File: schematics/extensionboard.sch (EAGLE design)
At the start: 25 parts, among them IC1 TXS0104E, IC2 TXS0104E, IC3 TXS0104E, IC4 TXS0104E, IC5 TXS0104E_ENA, J1 Raspberry Pi 3, J10 RPi_GPIO_2, J11 I2C_0, J12 SPI1_5V, J13 SDA1_5V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

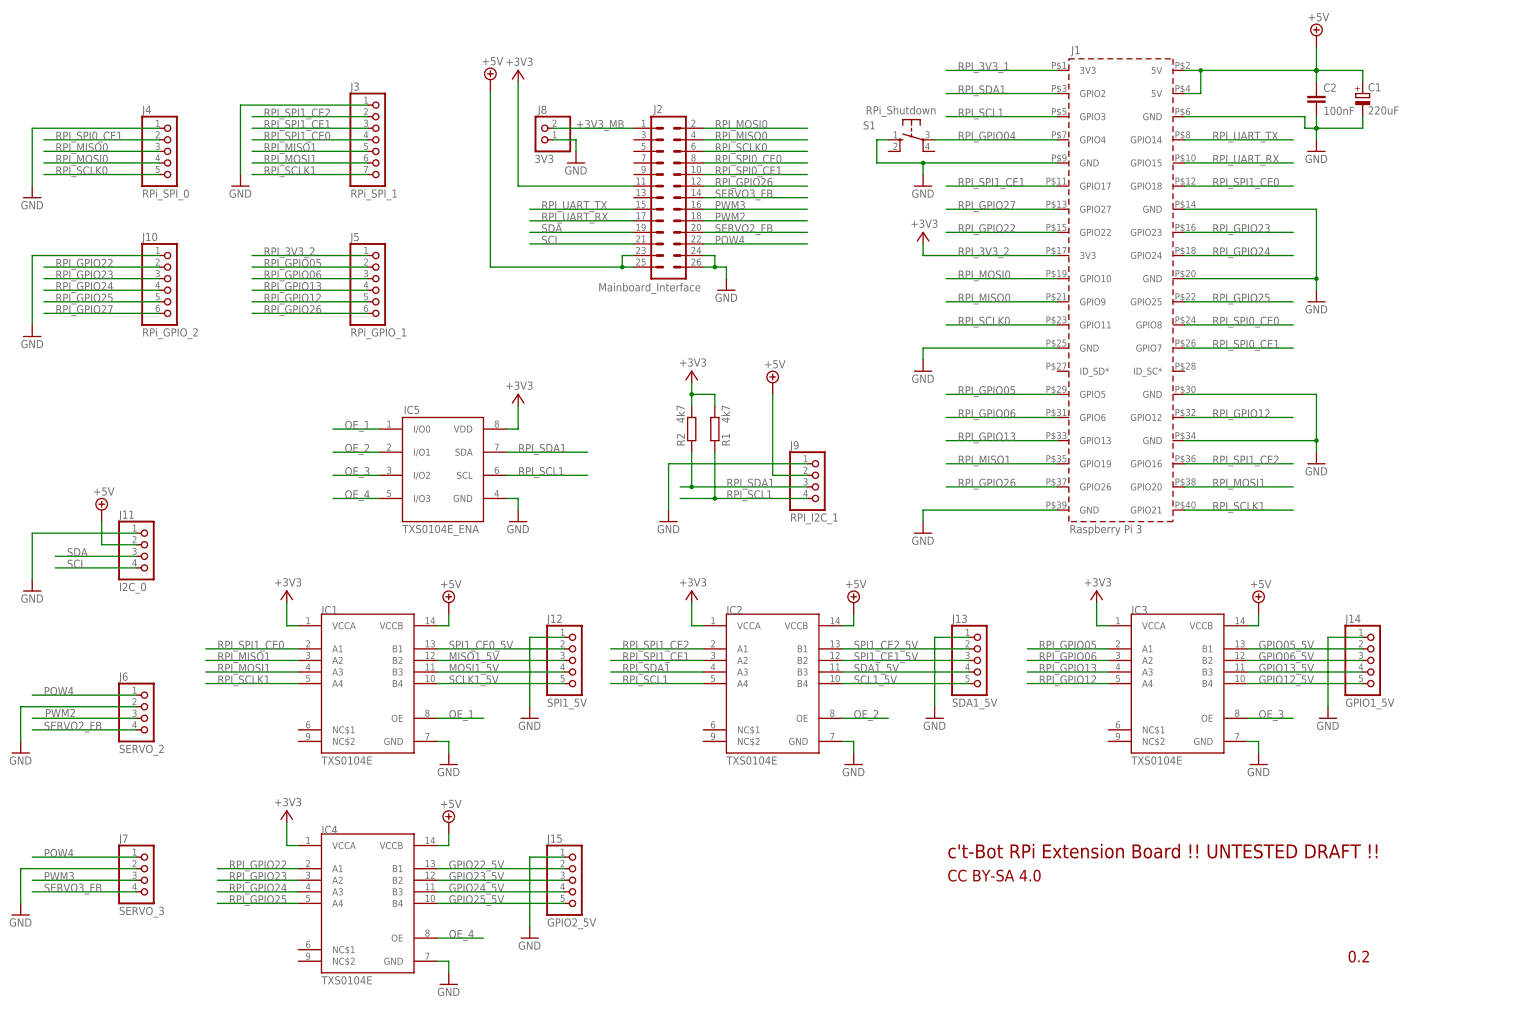
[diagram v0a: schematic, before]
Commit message: Servo PWM pullups corrected, battery voltage divider adjusted
schematic layout improved, signal names unified
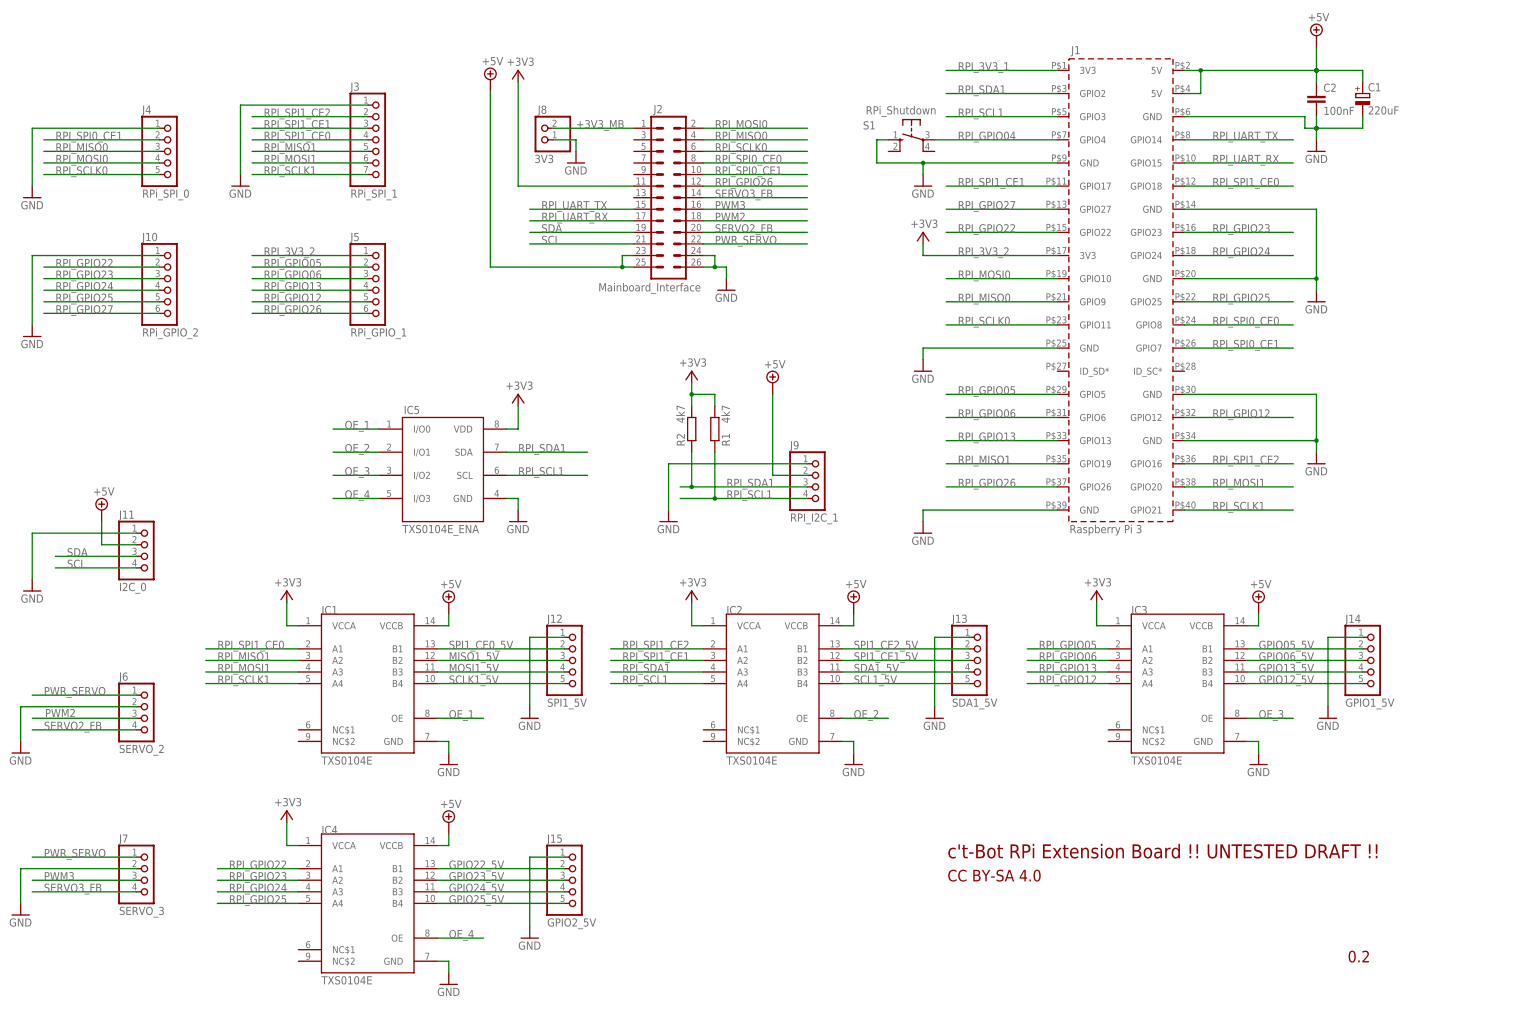
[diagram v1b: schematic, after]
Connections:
- net POW4 renamed PWR_SERVO
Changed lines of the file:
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@@
 </instance>
 <instance part="+3V6" gate="G$1" x="10.16" y="119.38" smashed="yes">
-<attribute name="VALUE" x="7.366" y="120.396" size="1.778" layer="96"/>
+<attribute name="VALUE" x="7.62" y="120.396" size="1.778" layer="96"/>
 </instance>
 <instance part="+3V7" gate="G$1" x="10.16" y="48.26" smashed="yes">
@@
 </segment>
 </net>
-<net name="POW4" class="0">
+<net name="PWR_SERVO" class="0">
 <segment>
 <pinref part="J7" gate="A" pin="1"/>

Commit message: schematics updated to rev 0.3
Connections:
- net GND: now also J6.1, J7.1; no longer J6.2, J7.2
- net GPIO12_5V: now also IC3.B3, J14.4; no longer IC3.B4, J14.5
- net GPIO13_5V: now also IC3.B4, J14.5; no longer IC3.B3, J14.4
- net PWR_SERVO: now also J6.2, J7.2; no longer J6.1, J7.1
- net RPI_GPIO12: now also IC3.A3, J5.4; no longer IC3.A4, J5.5
- net RPI_GPIO13: now also IC3.A4, J5.5; no longer IC3.A3, J5.4
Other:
- note added: "0.3"
- note removed: "0.2"
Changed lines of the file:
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@@
 <?xml version="1.0" encoding="utf-8"?>
 <!DOCTYPE eagle SYSTEM "eagle.dtd">
-<eagle version="8.6.3">
+<eagle version="8.7.1">
 <drawing>
 <settings>
@@
 <plain>
 <text x="104.394" y="-53.594" size="3.048" layer="94">c't-Bot RPi Extension Board !! UNTESTED DRAFT !!</text>
-<text x="192.278" y="-76.454" size="2.54" layer="94" font="vector">0.2</text>
+<text x="192.278" y="-76.454" size="2.54" layer="94" font="vector">0.3</text>
 <text x="104.394" y="-58.674" size="2.54" layer="94">CC BY-SA 4.0</text>
 </plain>
@@
 </segment>
 <segment>
-<pinref part="J7" gate="A" pin="2"/>
-<wire x1="-73.66" y1="-55.88" x2="-99.06" y2="-55.88" width="0.1524" layer="91"/>
 <pinref part="GND44" gate="1" pin="GND"/>
-<wire x1="-99.06" y1="-55.88" x2="-99.06" y2="-63.5" width="0.1524" layer="91"/>
-</segment>
-<segment>
-<pinref part="J6" gate="A" pin="2"/>
+<wire x1="-99.06" y1="-53.34" x2="-99.06" y2="-63.5" width="0.1524" layer="91"/>
+<pinref part="J7" gate="A" pin="1"/>
+<wire x1="-73.66" y1="-53.34" x2="-99.06" y2="-53.34" width="0.1524" layer="91"/>
+</segment>
+<segment>
 <pinref part="GND6" gate="1" pin="GND"/>
-<wire x1="-99.06" y1="-27.94" x2="-99.06" y2="-20.32" width="0.1524" layer="91"/>
-<wire x1="-99.06" y1="-20.32" x2="-73.66" y2="-20.32" width="0.1524" layer="91"/>
+<wire x1="-99.06" y1="-27.94" x2="-99.06" y2="-17.78" width="0.1524" layer="91"/>
+<pinref part="J6" gate="A" pin="1"/>
+<wire x1="-73.66" y1="-17.78" x2="-99.06" y2="-17.78" width="0.1524" layer="91"/>
 </segment>
 <segment>
@@
 <net name="RPI_GPIO12" class="0">
 <segment>
+<wire x1="156.464" y1="43.18" x2="180.34" y2="43.18" width="0.1524" layer="91"/>
+<label x="162.56" y="43.18" size="1.778" layer="95"/>
+<pinref part="J1" gate="G$1" pin="GPIO12"/>
+</segment>
+<segment>
+<pinref part="J5" gate="A" pin="4"/>
+<wire x1="-22.86" y1="71.12" x2="-48.26" y2="71.12" width="0.1524" layer="91"/>
+<label x="-45.72" y="71.12" size="1.778" layer="95"/>
+</segment>
+<segment>
+<pinref part="IC3" gate="G$1" pin="A3"/>
+<wire x1="139.7" y1="-12.7" x2="121.92" y2="-12.7" width="0.1524" layer="91"/>
+<label x="124.46" y="-12.7" size="1.778" layer="95"/>
+</segment>
+</net>
+<net name="RPI_GPIO05" class="0">
+<segment>
+<pinref part="J5" gate="A" pin="2"/>
+<wire x1="-22.86" y1="76.2" x2="-48.26" y2="76.2" width="0.1524" layer="91"/>
+<label x="-45.72" y="76.2" size="1.778" layer="95"/>
+</segment>
+<segment>
+<wire x1="128.524" y1="48.26" x2="104.14" y2="48.26" width="0.1524" layer="91"/>
+<label x="106.68" y="48.26" size="1.778" layer="95"/>
+<pinref part="J1" gate="G$1" pin="GPIO5"/>
+</segment>
+<segment>
+<pinref part="IC3" gate="G$1" pin="A1"/>
+<wire x1="139.7" y1="-7.62" x2="121.92" y2="-7.62" width="0.1524" layer="91"/>
+<label x="124.46" y="-7.62" size="1.778" layer="95"/>
+</segment>
+</net>
+<net name="RPI_GPIO06" class="0">
+<segment>
+<pinref part="J5" gate="A" pin="3"/>
+<wire x1="-22.86" y1="73.66" x2="-48.26" y2="73.66" width="0.1524" layer="91"/>
+<label x="-45.72" y="73.66" size="1.778" layer="95"/>
+</segment>
+<segment>
+<wire x1="128.524" y1="43.18" x2="104.14" y2="43.18" width="0.1524" layer="91"/>
+<label x="106.68" y="43.18" size="1.778" layer="95"/>
+<pinref part="J1" gate="G$1" pin="GPIO6"/>
+</segment>
+<segment>
+<pinref part="IC3" gate="G$1" pin="A2"/>
+<wire x1="139.7" y1="-10.16" x2="121.92" y2="-10.16" width="0.1524" layer="91"/>
+<label x="124.46" y="-10.16" size="1.778" layer="95"/>
+</segment>
+</net>
+<net name="RPI_GPIO13" class="0">
+<segment>
+<wire x1="128.524" y1="38.1" x2="104.14" y2="38.1" width="0.1524" layer="91"/>
+<label x="106.68" y="38.1" size="1.778" layer="95"/>
+<pinref part="J1" gate="G$1" pin="GPIO13"/>
+</segment>
+<segment>
 <pinref part="J5" gate="A" pin="5"/>
 <wire x1="-22.86" y1="68.58" x2="-48.26" y2="68.58" width="0.1524" layer="91"/>
@@
 </segment>
 <segment>
-<wire x1="156.464" y1="43.18" x2="180.34" y2="43.18" width="0.1524" layer="91"/>
-<label x="162.56" y="43.18" size="1.778" layer="95"/>
-<pinref part="J1" gate="G$1" pin="GPIO12"/>
-</segment>
-<segment>
 <pinref part="IC3" gate="G$1" pin="A4"/>
 <wire x1="139.7" y1="-15.24" x2="121.92" y2="-15.24" width="0.1524" layer="91"/>
 <label x="124.46" y="-15.24" size="1.778" layer="95"/>
-</segment>
-</net>
-<net name="RPI_GPIO05" class="0">
-<segment>
-<pinref part="J5" gate="A" pin="2"/>
-<wire x1="-22.86" y1="76.2" x2="-48.26" y2="76.2" width="0.1524" layer="91"/>
-<label x="-45.72" y="76.2" size="1.778" layer="95"/>
-</segment>
-<segment>
-<wire x1="128.524" y1="48.26" x2="104.14" y2="48.26" width="0.1524" layer="91"/>
-<label x="106.68" y="48.26" size="1.778" layer="95"/>
-<pinref part="J1" gate="G$1" pin="GPIO5"/>
-</segment>
-<segment>
-<pinref part="IC3" gate="G$1" pin="A1"/>
-<wire x1="139.7" y1="-7.62" x2="121.92" y2="-7.62" width="0.1524" layer="91"/>
-<label x="124.46" y="-7.62" size="1.778" layer="95"/>
-</segment>
-</net>
-<net name="RPI_GPIO06" class="0">
-<segment>
-<pinref part="J5" gate="A" pin="3"/>
-<wire x1="-22.86" y1="73.66" x2="-48.26" y2="73.66" width="0.1524" layer="91"/>
-<label x="-45.72" y="73.66" size="1.778" layer="95"/>
-</segment>
-<segment>
-<wire x1="128.524" y1="43.18" x2="104.14" y2="43.18" width="0.1524" layer="91"/>
-<label x="106.68" y="43.18" size="1.778" layer="95"/>
-<pinref part="J1" gate="G$1" pin="GPIO6"/>
-</segment>
-<segment>
-<pinref part="IC3" gate="G$1" pin="A2"/>
-<wire x1="139.7" y1="-10.16" x2="121.92" y2="-10.16" width="0.1524" layer="91"/>
-<label x="124.46" y="-10.16" size="1.778" layer="95"/>
-</segment>
-</net>
-<net name="RPI_GPIO13" class="0">
-<segment>
-<pinref part="J5" gate="A" pin="4"/>
-<wire x1="-22.86" y1="71.12" x2="-48.26" y2="71.12" width="0.1524" layer="91"/>
-<label x="-45.72" y="71.12" size="1.778" layer="95"/>
-</segment>
-<segment>
-<wire x1="128.524" y1="38.1" x2="104.14" y2="38.1" width="0.1524" layer="91"/>
-<label x="106.68" y="38.1" size="1.778" layer="95"/>
-<pinref part="J1" gate="G$1" pin="GPIO13"/>
-</segment>
-<segment>
-<pinref part="IC3" gate="G$1" pin="A3"/>
-<wire x1="139.7" y1="-12.7" x2="121.92" y2="-12.7" width="0.1524" layer="91"/>
-<label x="124.46" y="-12.7" size="1.778" layer="95"/>
 </segment>
 </net>
@@
 <net name="PWR_SERVO" class="0">
 <segment>
-<pinref part="J7" gate="A" pin="1"/>
-<wire x1="-73.66" y1="-53.34" x2="-96.52" y2="-53.34" width="0.1524" layer="91"/>
-<label x="-93.98" y="-53.34" size="1.778" layer="95"/>
-</segment>
-<segment>
-<pinref part="J6" gate="A" pin="1"/>
-<wire x1="-73.66" y1="-17.78" x2="-96.52" y2="-17.78" width="0.1524" layer="91"/>
-<label x="-93.98" y="-17.78" size="1.778" layer="95"/>
-</segment>
-<segment>
 <pinref part="J2" gate="1" pin="22"/>
 <wire x1="50.8" y1="81.28" x2="73.66" y2="81.28" width="0.1524" layer="91"/>
 <label x="53.34" y="81.28" size="1.778" layer="95"/>
+</segment>
+<segment>
+<pinref part="J6" gate="A" pin="2"/>
+<wire x1="-73.66" y1="-20.32" x2="-96.52" y2="-20.32" width="0.1524" layer="91"/>
+<label x="-93.98" y="-20.32" size="1.778" layer="95"/>
+</segment>
+<segment>
+<pinref part="J7" gate="A" pin="2"/>
+<wire x1="-73.66" y1="-55.88" x2="-96.52" y2="-55.88" width="0.1524" layer="91"/>
+<label x="-93.98" y="-55.88" size="1.778" layer="95"/>
 </segment>
 </net>
@@
 </segment>
 </net>
-<net name="GPIO13_5V" class="0">
+<net name="GPIO12_5V" class="0">
 <segment>
 <pinref part="IC3" gate="G$1" pin="B3"/>
@@
 </segment>
 </net>
-<net name="GPIO12_5V" class="0">
+<net name="GPIO13_5V" class="0">
 <segment>
 <pinref part="IC3" gate="G$1" pin="B4"/>
